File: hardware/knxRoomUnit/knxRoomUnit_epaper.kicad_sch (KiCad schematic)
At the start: 24 parts, among them P1 ePaper FL, P2 ePaper, Q3 SI1308

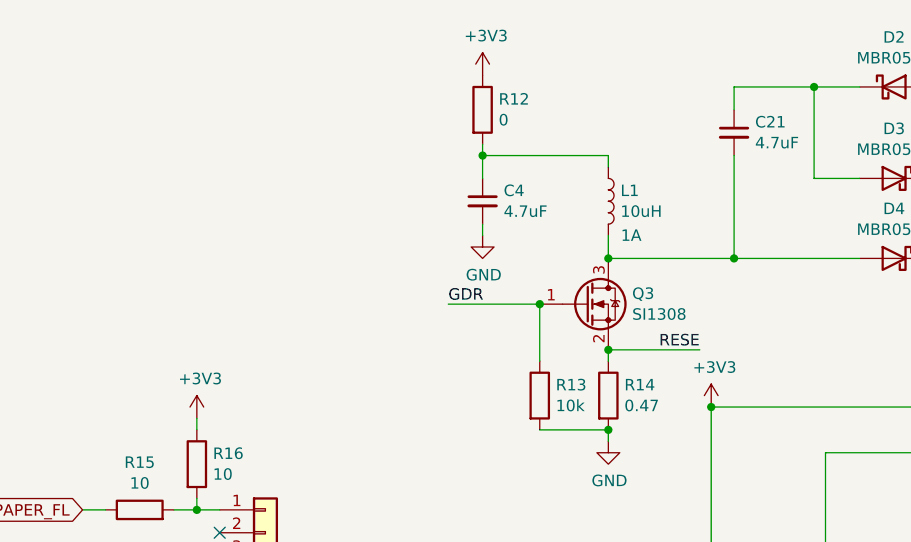
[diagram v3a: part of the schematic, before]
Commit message: Updated HW design
Flipped P1 to match display's pinout
Changed 0201 resistors to 0603
Added R12 to section 3V3 to display
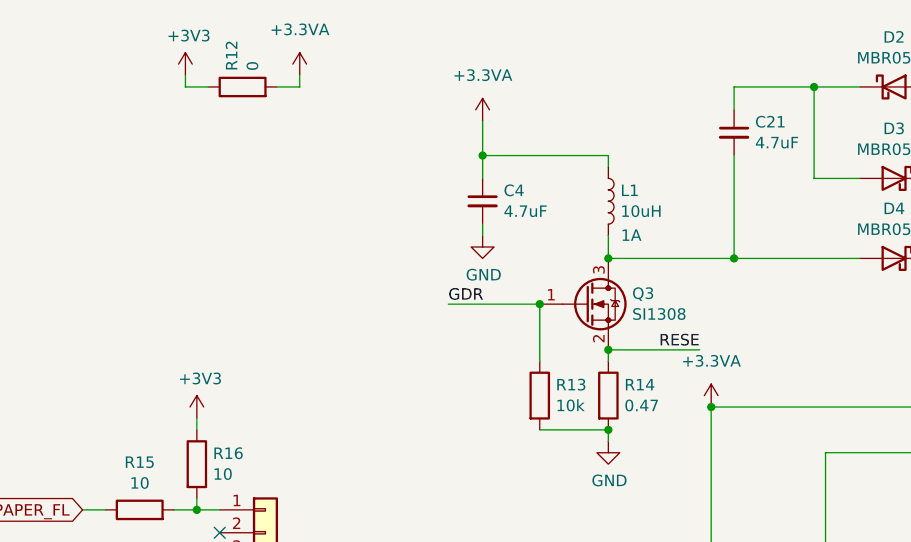
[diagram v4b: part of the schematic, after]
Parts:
- P1: LCSC Part # (none) -> C2842522; Manufacturer (none) -> JUSHUO; PartNumber (none) -> AFC34-S06FIA-00; now in the parts list
- P2: LCSC Part # (none) -> C2842527; Manufacturer (none) -> JUSHUO; PartNumber (none) -> AFC34-S24FIA-00; now in the parts list
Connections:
- net +3V3: no longer C8.1, P2.15 (Pin_15), P2.16 (Pin_16)
- net +3.3VA: now reaches C4.1, L1.1, R12.2
- net +3.3VA: now also C8.1, P2.15 (Pin_15), P2.16 (Pin_16)
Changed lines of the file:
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@@
   (title_block
     (title "knxRoomUnit")
-    (date "2023-08-22")
-    (rev "r1d0")
+    (date "2024-01-21")
+    (rev "r1d1")
     (company "MP")
   )
@@
   (junction (at 144.78 59.69) (diameter 0) (color 0 0 0 0)
   )
+  (junction (at 133.35 95.25) (diameter 0) (color 0 0 0 0)
+  )
   (junction (at 114.3 83.82) (diameter 0) (color 0 0 0 0)
   )
@@
   )
   (junction (at 226.06 123.19) (diameter 0) (color 0 0 0 0)
-  )
-  (junction (at 133.35 95.25) (diameter 0) (color 0 0 0 0)
   )
   (junction (at 196.85 123.19) (diameter 0) (color 0 0 0 0)
@@
     (stroke (width 0) (type default))
   )
+  (wire (pts (xy 74.93 59.69) (xy 74.93 58.42))
+    (stroke (width 0) (type default))
+  )
+  (wire (pts (xy 87.63 59.69) (xy 85.09 59.69))
+    (stroke (width 0) (type default))
+  )
   (wire (pts (xy 132.08 88.9) (xy 121.92 88.9))
     (stroke (width 0) (type default))
@@
     (stroke (width 0) (type default))
   )
+  (wire (pts (xy 77.47 59.69) (xy 74.93 59.69))
+    (stroke (width 0) (type default))
+  )
   (wire (pts (xy 76.2 106.68) (xy 78.74 106.68))
     (stroke (width 0) (type default))
@@
     (stroke (width 0) (type default))
   )
+  (wire (pts (xy 87.63 58.42) (xy 87.63 59.69))
+    (stroke (width 0) (type default))
+  )
   (wire (pts (xy 226.06 123.19) (xy 226.06 97.79))
     (stroke (width 0) (type default))
@@
     (stroke (width 0) (type default))
   )
-  (wire (pts (xy 107.95 67.31) (xy 107.95 66.04))
+  (wire (pts (xy 107.95 67.31) (xy 107.95 63.5))
     (stroke (width 0) (type default))
   )
@@
   )
   (symbol (lib_id "Connector_Generic:Conn_01x24") (at 232.41 85.09 0) (unit 1)
-    (in_bom no) (on_board yes) (dnp no)
+    (in_bom yes) (on_board yes) (dnp no)
     (property "Reference" "P2" (at 234.442 85.2932 0)
       (effects (font (size 1.27 1.27)) (justify left))
@@
       (effects (font (size 1.27 1.27)) hide)
     )
-    (property "Datasheet" "" (at 232.41 85.09 0)
+    (property "Datasheet" "https://datasheet.lcsc.com/lcsc/2304140030_JUSHUO-AFC34-S24FIA-00_C2842527.pdf" (at 232.41 85.09 0)
+      (effects (font (size 1.27 1.27)) hide)
+    )
+    (property "LCSC Part #" "C2842527" (at 232.41 85.09 0)
+      (effects (font (size 1.27 1.27)) hide)
+    )
+    (property "Manufacturer" "JUSHUO" (at 232.41 85.09 0)
+      (effects (font (size 1.27 1.27)) hide)
+    )
+    (property "PartNumber" "AFC34-S24FIA-00" (at 232.41 85.09 0)
       (effects (font (size 1.27 1.27)) hide)
     )
@@
     )
   )
-  (symbol (lib_id "power:+3V3") (at 133.35 95.25 0) (unit 1)
-    (in_bom yes) (on_board yes) (dnp no)
-    (property "Reference" "#PWR058" (at 133.35 99.06 0)
-      (effects (font (size 1.27 1.27)) hide)
-    )
-    (property "Value" "+3V3" (at 133.731 90.8558 0)
-      (effects (font (size 1.27 1.27)))
-    )
-    (property "Footprint" "" (at 133.35 95.25 0)
-      (effects (font (size 1.27 1.27)) hide)
-    )
-    (property "Datasheet" "" (at 133.35 95.25 0)
-      (effects (font (size 1.27 1.27)) hide)
-    )
-    (pin "1")
-    (instances
-      (project "knxRoomUnit"
-        (path "/699feae1-8cdd-4d2b-947f-f24849c73cdb/00000000-0000-0000-0000-00006041ea0b"
-          (reference "#PWR058") (unit 1)
-        )
-      )
-    )
-  )
   (symbol (lib_id "Device:C_Small") (at 135.89 64.77 0) (mirror y) (unit 1)
     (in_bom yes) (on_board yes) (dnp no)
@@
     )
   )
-  (symbol (lib_id "power:+3V3") (at 107.95 58.42 0) (unit 1)
-    (in_bom yes) (on_board yes) (dnp no)
-    (property "Reference" "#PWR055" (at 107.95 62.23 0)
-      (effects (font (size 1.27 1.27)) hide)
-    )
-    (property "Value" "+3V3" (at 108.331 54.0258 0)
-      (effects (font (size 1.27 1.27)))
-    )
-    (property "Footprint" "" (at 107.95 58.42 0)
-      (effects (font (size 1.27 1.27)) hide)
-    )
-    (property "Datasheet" "" (at 107.95 58.42 0)
+  (symbol (lib_id "power:+3V3") (at 74.93 58.42 0) (unit 1)
+    (in_bom yes) (on_board yes) (dnp no)
+    (property "Reference" "#PWR055" (at 74.93 62.23 0)
+      (effects (font (size 1.27 1.27)) hide)
+    )
+    (property "Value" "+3V3" (at 75.311 54.0258 0)
+      (effects (font (size 1.27 1.27)))
+    )
+    (property "Footprint" "" (at 74.93 58.42 0)
+      (effects (font (size 1.27 1.27)) hide)
+    )
+    (property "Datasheet" "" (at 74.93 58.42 0)
       (effects (font (size 1.27 1.27)) hide)
     )
@@
   )
   (symbol (lib_id "Connector_Generic:Conn_01x06") (at 83.82 111.76 0) (unit 1)
-    (in_bom no) (on_board yes) (dnp no)
+    (in_bom yes) (on_board yes) (dnp no)
     (property "Reference" "P1" (at 85.852 111.9632 0)
       (effects (font (size 1.27 1.27)) (justify left))
@@
       (effects (font (size 1.27 1.27)) hide)
     )
-    (property "Datasheet" "" (at 83.82 111.76 0)
+    (property "Datasheet" "https://datasheet.lcsc.com/lcsc/2304140030_JUSHUO-AFC34-S24FIA-00_C2842527.pdf" (at 83.82 111.76 0)
+      (effects (font (size 1.27 1.27)) hide)
+    )
+    (property "LCSC Part #" "C2842522" (at 83.82 111.76 0)
+      (effects (font (size 1.27 1.27)) hide)
+    )
+    (property "Manufacturer" "JUSHUO" (at 83.82 111.76 0)
+      (effects (font (size 1.27 1.27)) hide)
+    )
+    (property "PartNumber" "AFC34-S06FIA-00" (at 83.82 111.76 0)
       (effects (font (size 1.27 1.27)) hide)
     )
@@
     )
   )
-  (symbol (lib_id "Device:R") (at 107.95 62.23 0) (unit 1)
-    (in_bom yes) (on_board yes) (dnp no)
-    (property "Reference" "R12" (at 109.728 61.0616 0)
-      (effects (font (size 1.27 1.27)) (justify left))
-    )
-    (property "Value" "0" (at 109.728 63.373 0)
-      (effects (font (size 1.27 1.27)) (justify left))
-    )
-    (property "Footprint" "Resistor_SMD:R_0805_2012Metric" (at 106.172 62.23 90)
-      (effects (font (size 1.27 1.27)) hide)
-    )
-    (property "Datasheet" "https://datasheet.lcsc.com/lcsc/2206010216_UNI-ROYAL-Uniroyal-Elec-0805W8F0000T5E_C17477.pdf" (at 107.95 62.23 0)
-      (effects (font (size 1.27 1.27)) hide)
-    )
-    (property "LCSC Part #" "C17477" (at 107.95 62.23 0)
-      (effects (font (size 1.27 1.27)) hide)
-    )
-    (property "Manufacturer" "UNI-ROYAL(Uniroyal Elec)" (at 107.95 62.23 0)
-      (effects (font (size 1.27 1.27)) hide)
-    )
-    (property "PartNumber" "0805W8F0000T5E" (at 107.95 62.23 0)
-      (effects (font (size 1.27 1.27)) hide)
-    )
+  (symbol (lib_id "power:+3.3VA") (at 133.35 95.25 0) (unit 1)
+    (in_bom yes) (on_board yes) (dnp no) (fields_autoplaced)
+    (property "Reference" "#PWR08" (at 133.35 99.06 0)
+      (effects (font (size 1.27 1.27)) hide)
+    )
+    (property "Value" "+3.3VA" (at 133.35 90.17 0)
+      (effects (font (size 1.27 1.27)))
+    )
+    (property "Footprint" "" (at 133.35 95.25 0)
+      (effects (font (size 1.27 1.27)) hide)
+    )
+    (property "Datasheet" "" (at 133.35 95.25 0)
+      (effects (font (size 1.27 1.27)) hide)
+    )
+    (pin "1")
+    (instances
+      (project "knxRoomUnit"
+        (path "/699feae1-8cdd-4d2b-947f-f24849c73cdb/00000000-0000-0000-0000-00006041ea0b"
+          (reference "#PWR08") (unit 1)
+        )
+      )
+    )
+  )
+  (symbol (lib_id "power:+3.3VA") (at 87.63 58.42 0) (unit 1)
+    (in_bom yes) (on_board yes) (dnp no) (fields_autoplaced)
+    (property "Reference" "#PWR06" (at 87.63 62.23 0)
+      (effects (font (size 1.27 1.27)) hide)
+    )
+    (property "Value" "+3.3VA" (at 87.63 53.34 0)
+      (effects (font (size 1.27 1.27)))
+    )
+    (property "Footprint" "" (at 87.63 58.42 0)
+      (effects (font (size 1.27 1.27)) hide)
+    )
+    (property "Datasheet" "" (at 87.63 58.42 0)
+      (effects (font (size 1.27 1.27)) hide)
+    )
+    (pin "1")
+    (instances
+      (project "knxRoomUnit"
+        (path "/699feae1-8cdd-4d2b-947f-f24849c73cdb/00000000-0000-0000-0000-00006041ea0b"
+          (reference "#PWR06") (unit 1)
+        )
+      )
+    )
+  )
+  (symbol (lib_id "power:+3.3VA") (at 107.95 63.5 0) (unit 1)
+    (in_bom yes) (on_board yes) (dnp no) (fields_autoplaced)
+    (property "Reference" "#PWR07" (at 107.95 67.31 0)
+      (effects (font (size 1.27 1.27)) hide)
+    )
+    (property "Value" "+3.3VA" (at 107.95 58.42 0)
+      (effects (font (size 1.27 1.27)))
+    )
+    (property "Footprint" "" (at 107.95 63.5 0)
+      (effects (font (size 1.27 1.27)) hide)
+    )
+    (property "Datasheet" "" (at 107.95 63.5 0)
+      (effects (font (size 1.27 1.27)) hide)
+    )
+    (pin "1")
+    (instances
+      (project "knxRoomUnit"
+        (path "/699feae1-8cdd-4d2b-947f-f24849c73cdb/00000000-0000-0000-0000-00006041ea0b"
+          (reference "#PWR07") (unit 1)
+        )
+      )
+    )
+  )
+  (symbol (lib_id "Device:R") (at 81.28 59.69 90) (unit 1)
+    (in_bom yes) (on_board yes) (dnp no)
+    (property "Reference" "R12" (at 80.1116 57.912 0)
+      (effects (font (size 1.27 1.27)) (justify left))
+    )
+    (property "Value" "0" (at 82.423 57.912 0)
+      (effects (font (size 1.27 1.27)) (justify left))
+    )
+    (property "Footprint" "Resistor_SMD:R_0805_2012Metric" (at 81.28 61.468 90)
+      (effects (font (size 1.27 1.27)) hide)
+    )
+    (property "Datasheet" "https://datasheet.lcsc.com/lcsc/2206010216_UNI-ROYAL-Uniroyal-Elec-0805W8F0000T5E_C17477.pdf" (at 81.28 59.69 0)
+      (effects (font (size 1.27 1.27)) hide)
+    )
+    (property "LCSC Part #" "C17477" (at 81.28 59.69 0)
+      (effects (font (size 1.27 1.27)) hide)
+    )
+    (property "Manufacturer" "UNI-ROYAL(Uniroyal Elec)" (at 81.28 59.69 0)
+      (effects (font (size 1.27 1.27)) hide)
+    )
+    (property "PartNumber" "0805W8F0000T5E" (at 81.28 59.69 0)
+      (effects (font (size 1.27 1.27)) hide)
+    )
